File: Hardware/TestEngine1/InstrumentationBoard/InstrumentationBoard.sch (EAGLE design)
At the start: 43 parts, among them IC1 MAX31855, J1 1X2-3.5MM

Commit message: added user interface and saftey interlocks.
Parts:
- added C10, C12, C8: 0.1uF, SparkFun-Capacitors:CAP0805
- added C11: 0.33uF, SparkFun-Capacitors:CAP0805
- added JP10, JP11, JP14, JP15, JP16: (no value), SparkFun-Connectors:M03PTH
- added JP12: (no value), SparkFun-Connectors:M04PTH
- added JP13: (no value), SparkFun-Connectors:M05PTH
- added JP17: M02PTH, SparkFun-Connectors:M02PTH
- added LED1: RGBLED5050, adafruit:RGBLED5050
- added Q1, Q2, Q3: MOSFET-NCHANNELBSS123LT1G, SparkFun-DiscreteSemi:MOSFET-NCHANNELBSS123LT1G
- added R12: 33, SparkFun-Resistors:RESISTOR0805-RES
- added R13: 66, SparkFun-Resistors:RESISTOR0805-RES
- added R14: 68, adafruit:R-US_R0805
- added R15, R16: 0, adafruit:R-US_R0805
- added R17, R18, R19, R20, R21: 10K, adafruit:R-US_R0805
- added S1: SWITCH-MOMENTARY-2SMD, SparkFun-Electromechanical:SWITCH-MOMENTARY-2SMD
- added U$8: MC33269DTRK, RitLaunchInitiative:MC33269DTRK
- added U1: BMP180, SparkFun-Sensors:BMP180
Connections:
- net THERMOCOUPLE renamed LOADCELL
- removed net DO: IC1.DO
- new net BLUE: Q1.G, R17.1
- new net GREEN: Q2.G, R18.1
- new net MISO: IC1.DO, JP13.5
- new net MOSI: JP13.4
- new net N$10: LED1.GREEN_A, R15.2
- new net N$15: LED1.BLUE_A, R16.2
- new net N$2: JP10.2, R12.2
- new net N$3: LED1.RED_C, Q3.D
- new net N$7: LED1.GREEN_C, Q2.D
- new net N$8: LED1.BLUE_C, Q1.D
- new net N$9: LED1.RED_A, R14.2
- new net PSI_1: R12.1, R13.2
- new net PSI_2_CS: JP13.2
- new net PWM_1: JP14.1
- new net PWM_2: JP15.1
- new net PWM_3: JP16.1
- new net RED: Q3.G, R19.1
- new net SCL: JP11.2, U1.SCL
- new net SCLK: D1.C, JP13.3
- new net SDA: JP11.3, U1.SDA
- new net SW_1: R20.1, S1.1
- new net THERMOCOUPLE_CS: D2.C
- new net TILTSWITCH_1: JP17.1, R21.1
- net +3V3: now also C10.1, C8.1, JP12.2, JP17.2, R14.1, R15.1, R16.1, S1.2, U1.VDD, U1.VDDIO
- net 12V: now also C11.1, JP12.4, U$8.IN
- net 5V: now also C12.1, JP10.1, JP12.3, JP14.2, JP15.2, JP16.2, U$8.OUT
- net CS: no longer D2.C
- net GND: now also C10.2, C8.2, JP10.3, JP11.1, JP12.1, JP13.1, JP14.3, JP15.3, JP16.3, Q1.S, Q2.S, Q3.S, R13.1, R17.2, R18.2, R19.2, R20.2, R21.2, U1.GND
- net N$12: now also C11.2, C12.2, U$8.GND
- net SCK: no longer D1.C
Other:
- note added: "160-2022-1-ND"
- note added: "5v Pressure transducer"
- note added: "Barometric Pressure Sensor"
- note added: "Current feedback Pressure transducer"
- note added: "Excite +"
- note added: "Excite -"
- note added: "I2c"
- note added: "K type Thermocouple"
- note added: "Load Cell"
- note added: "Optional for additional current sink"
- note added: "Scale signal from 5v to 3.3"
- note added: "Tilt Switch"
- note added: "V+"
- note added: "V-"
- moved on the sheet: C4, C5, C6, C7, C9, J2, J3, JP1, JP2, JP3, JP4, JP5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

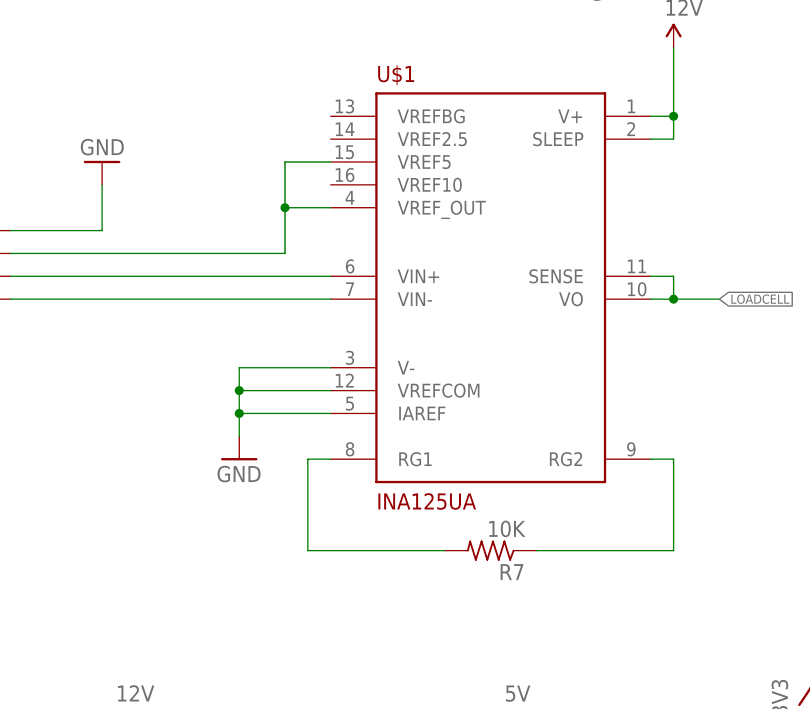
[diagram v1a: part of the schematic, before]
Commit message: routed alternet Pressure sense adapter board
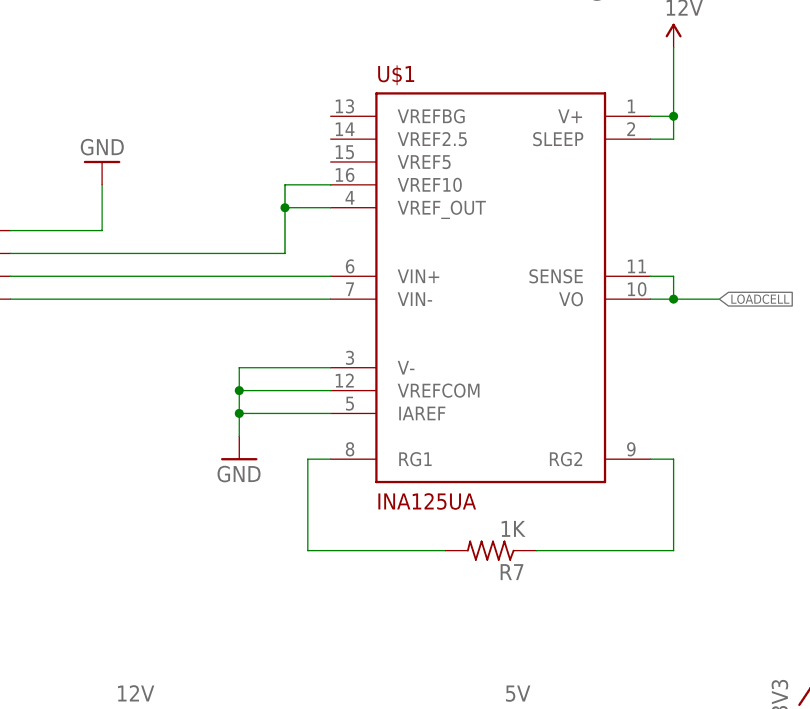
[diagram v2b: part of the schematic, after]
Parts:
- R7: value 10K -> 1K
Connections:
- net N$20: now also U$1.VREF10; no longer U$1.VREF5
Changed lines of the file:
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@@
 <part name="C6" library="SparkFun-Capacitors" deviceset="CAP" device="0805" value="1uF"/>
 <part name="C7" library="SparkFun-Capacitors" deviceset="CAP" device="0805" value="1uF"/>
-<part name="R7" library="adafruit" deviceset="R-US_" device="R0805" value="10K"/>
+<part name="R7" library="adafruit" deviceset="R-US_" device="R0805" value="1K"/>
 <part name="SUPPLY2" library="SparkFun-Aesthetics" deviceset="12V" device=""/>
 <part name="SUPPLY3" library="SparkFun-Aesthetics" deviceset="12V" device=""/>
@@
 <net name="N$20" class="0">
 <segment>
-<pinref part="U$1" gate="G$1" pin="VREF5"/>
-<wire x1="-93.98" y1="66.04" x2="-99.06" y2="66.04" width="0.1524" layer="91"/>
-<wire x1="-99.06" y1="66.04" x2="-99.06" y2="60.96" width="0.1524" layer="91"/>
+<wire x1="-99.06" y1="63.5" x2="-99.06" y2="60.96" width="0.1524" layer="91"/>
 <pinref part="U$1" gate="G$1" pin="VREF_OUT"/>
 <wire x1="-99.06" y1="60.96" x2="-93.98" y2="60.96" width="0.1524" layer="91"/>
@@
 <pinref part="JP5" gate="G$1" pin="3"/>
 <wire x1="-129.54" y1="55.88" x2="-99.06" y2="55.88" width="0.1524" layer="91"/>
-</segment>
-</net>
+<pinref part="U$1" gate="G$1" pin="VREF10"/>
+<wire x1="-93.98" y1="63.5" x2="-99.06" y2="63.5" width="0.1524" layer="91"/>
+</segment>
+</net>

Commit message: added various components
extra bulk capacitance
power leds
battery voltage measurement
added extra analog channels
Back EMF protection diodes
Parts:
- added C13, C16: 10uF, SparkFun-Capacitors:CAP0805
- added C14, C17, C19: 0.1uf, SparkFun-Capacitors:CAP0805
- added C15, C18: 100pF, SparkFun-Capacitors:CAP0805
- added D3, D4, D5, D6: B340A, SparkFun-DiscreteSemi:DIODE-SCHOTTKY-B340A
- added D7, D8, D9: (no value), SparkFun-LED:LED1206
- added JP18: M02PTH, SparkFun-Connectors:M02PTH
- added JP19, JP20: (no value), SparkFun-Connectors:M03PTH
- added R22: 9k, adafruit:R-US_R0805
- added R23: 3k, adafruit:R-US_R0805
- added R24: 10k, SparkFun-Resistors:RESISTOR0805-RES
- added R25: 1.7k, SparkFun-Resistors:RESISTOR0805-RES
- added R26: 3.3k, SparkFun-Resistors:RESISTOR0805-RES
- added R27: 100, adafruit:R-US_R0805
- added R28: 220, adafruit:R-US_R0805
- added R29: 680, adafruit:R-US_R0805
- R12: value 33 -> 1.7k
- R13: value 66 -> 3.3k
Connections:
- removed net MOSI: JP13.4
- removed net PSI_2_CS: JP13.2
- new net BATTVOLTAGE: R22.2, R23.1
- new net N$21: JP19.2, R25.2
- new net N$23: D7.A, R28.2
- new net N$24: D8.A, R27.2
- new net N$25: D9.A, R29.2
- new net PSI_2: R25.1, R26.2
- new net PWM_4: JP20.1
- new net TR5: JP18.1, R24.2
- net +3V3: now also C19.2, JP18.2, R27.1
- net 12V: now also C13.1, C14.1, C15.1, C16.1, C17.1, C18.1, JP13.5, R22.1, R29.1
- net 5V: now also JP19.1, JP20.2, R28.1
- net GND: now also C13.2, C14.2, C15.2, C16.2, C17.2, C18.2, C19.1, D3.A, D4.A, D5.A, D6.A, D7.C, D8.C, D9.C, JP13.3, JP13.4, JP19.3, JP20.3, R23.2, R24.1, R26.1; no longer JP13.1
- net MISO: no longer JP13.5
- net N$17: now also D6.C
- net N$18: now also D3.C
- net N$19: now also D4.C
- net N$22: now also D5.C
- net SCL: now also JP13.2
- net SCLK: no longer JP13.3
- net SDA: now also JP13.1
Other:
- note added: "3.3v LDO"
- note added: "5v LDO"
- note added: "Load Cell measurement"
- note added: "Power supply section"
- note added: "Pressure transducers voltage signaling"
- note added: "Servos. optional*"
- note added: "Thermistors"
- note added: "battery voltage measurment"
- note removed: "Load Cell"
- moved on the sheet: C11, C12, JP1, JP10, JP11, JP12, JP13, JP14, JP15, JP16, JP2, JP3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
